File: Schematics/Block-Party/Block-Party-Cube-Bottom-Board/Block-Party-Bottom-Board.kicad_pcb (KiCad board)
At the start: 2 copper layers, 40 x 40 mm, 10 parts

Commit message: Revision 1.01 of the PCBs
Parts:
- removed J1, J2, J3, J4: ~, Connector_PinHeader_2.54mm:PinHeader_1x01_P2.54mm_Vertical
- added J6: YTC-A1001LF-04A, adafruit-jst-4328:ADAFRUIT_4328, F.Cu at (159.2, 77.3)
- added TP1: Diode5V, TestPoint:TestPoint_Pad_D1.0mm, F.Cu at (170.7, 80.6)
- added TP2: DODI, TestPoint:TestPoint_Pad_D1.0mm, F.Cu at (155.2, 81.1)
- added TP4: DO, TestPoint:TestPoint_Pad_D1.0mm, F.Cu at (161.7, 82.1)
- added TP5: 5V, TestPoint:TestPoint_Pad_D1.0mm, F.Cu at (161.7, 86.6)
- added TP6: DI, TestPoint:TestPoint_Pad_D1.0mm, F.Cu at (152.7, 79.1)
- moved LED1 10.4 mm to (159.2, 82.6), turned to -90 degrees
- moved D1 10.0 mm to (168.2, 78.1)
- moved R1 9.49 mm to (164.2, 80.6), turned to 90 degrees
- moved LED2 7.90 mm to (159.4, 73.1), turned to -90 degrees
- moved C1 6.04 mm to (165.2, 76.6), turned to 180 degrees
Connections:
- J5 pad 5: (no net) -> unconnected-(J5-HOLE-Pad5)_1
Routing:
- net D5V: track 64.5 -> 24.6 mm
- net Net-(LED1-DI): track 52.4 -> 15.4 mm
- net DIN: track 48.3 -> 15.2 mm, vias 0 -> 2
- net DOUT: track 33.9 -> 2.77 mm
- net +5V: track 47.4 -> 20.6 mm
- net SENSE: track 43.4 -> 22.4 mm, vias 0 -> 2
- net GND: track 6.66 -> 23.5 mm
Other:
- outline, holes or cut-outs redrawn

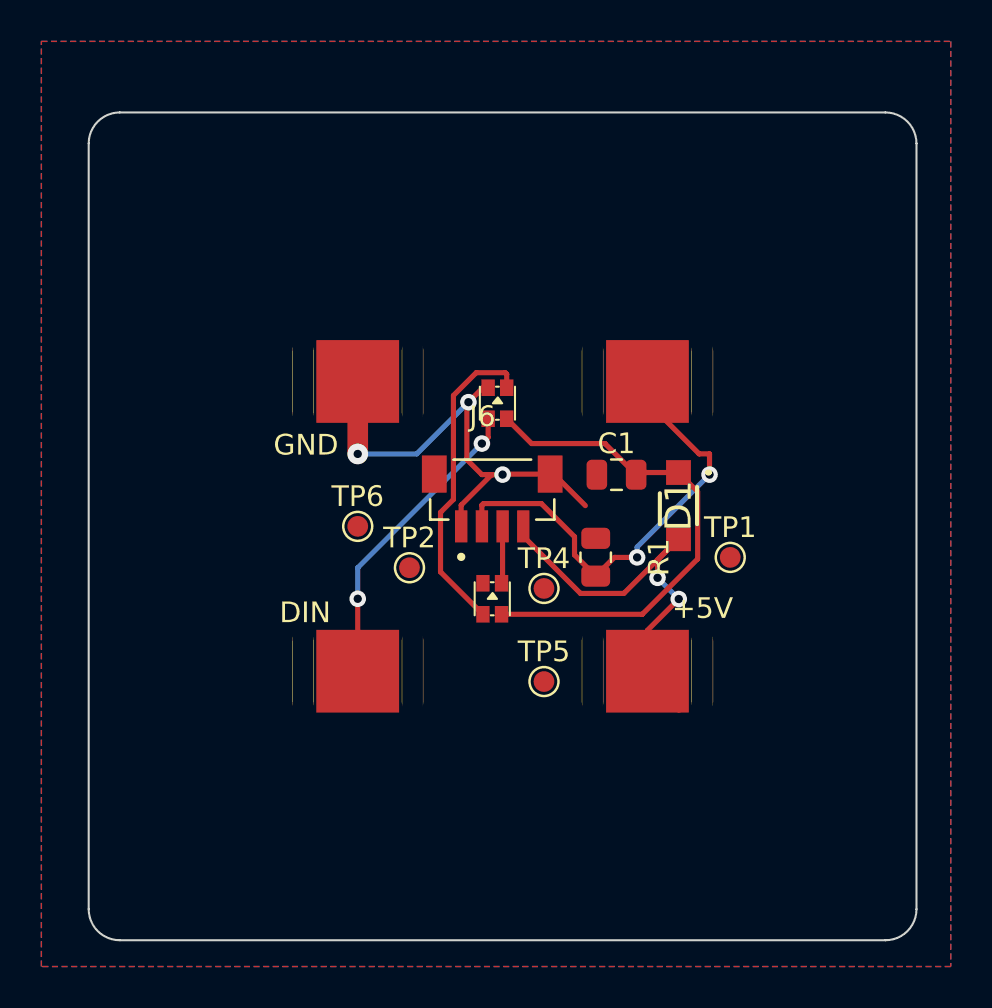
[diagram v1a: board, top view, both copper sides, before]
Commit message: Found a good jst part number and updated the BOMs
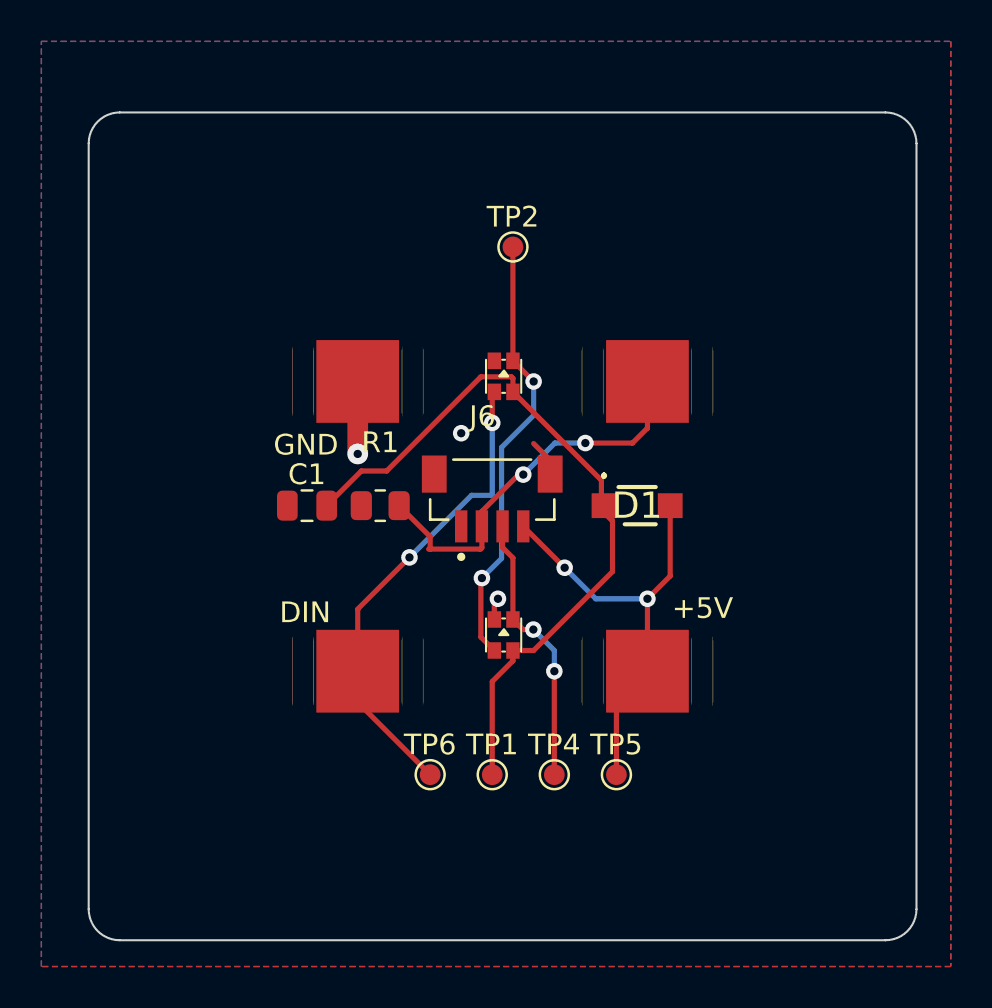
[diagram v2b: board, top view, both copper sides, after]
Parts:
- moved TP2 16.3 mm to (160.2, 65.6)
- moved TP1 15.6 mm to (159.2, 91.1)
- moved C1 15.0 mm to (150.2, 78.1)
- moved TP6 12.5 mm to (156.2, 91.1)
- moved R1 10.7 mm to (153.8, 78.1), turned to 180 degrees
- moved TP4 9.01 mm to (162.2, 91.1)
- moved TP5 5.70 mm to (165.2, 91.1)
- moved D1 2.00 mm to (166.2, 78.1), turned to 0 degrees
- moved LED1 1.83 mm to (159.8, 84.3)
- moved LED2 1.33 mm to (159.8, 71.8)
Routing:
- net GND: track 23.5 -> 5.63 mm
- net D5V: track 24.6 -> 35.8 mm
- net DOUT: track 2.77 -> 13.3 mm, vias 0 -> 2
- net DIN: track 15.2 -> 23.3 mm
- net Net-(LED1-DI): track 15.4 -> 21.2 mm, vias 0 -> 2
- net SENSE: track 22.4 -> 19.0 mm
- net +5V: track 20.6 -> 23.7 mm

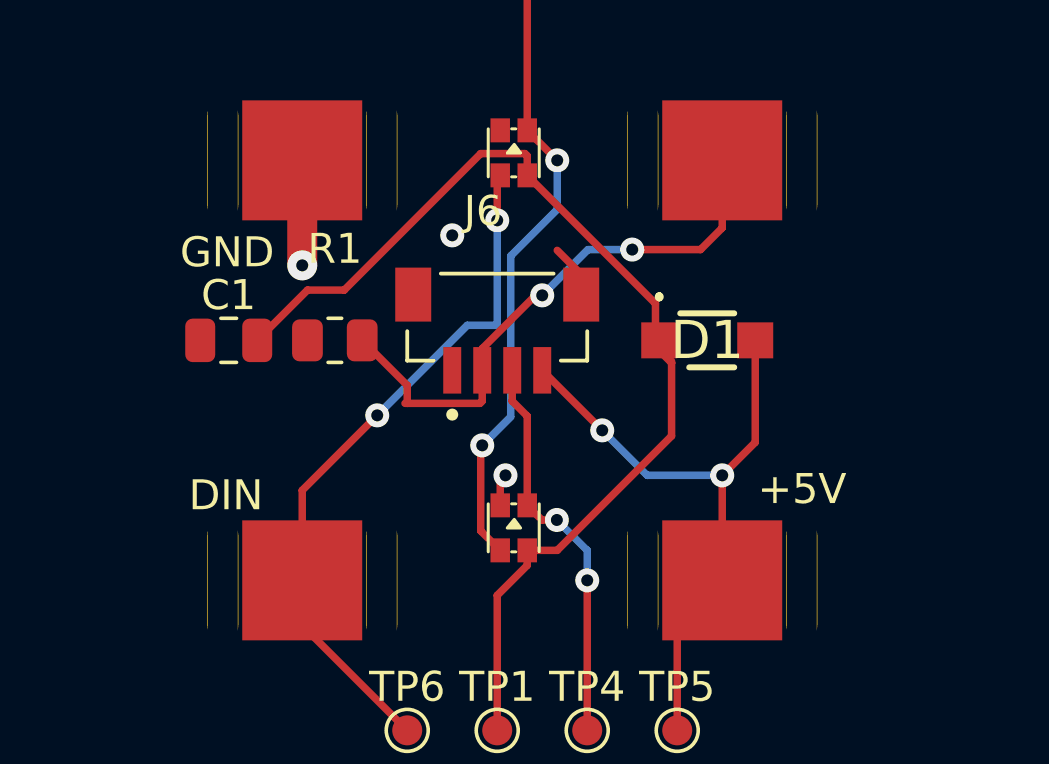
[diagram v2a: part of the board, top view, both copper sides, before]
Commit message: Made the top and bottom PCB the same size
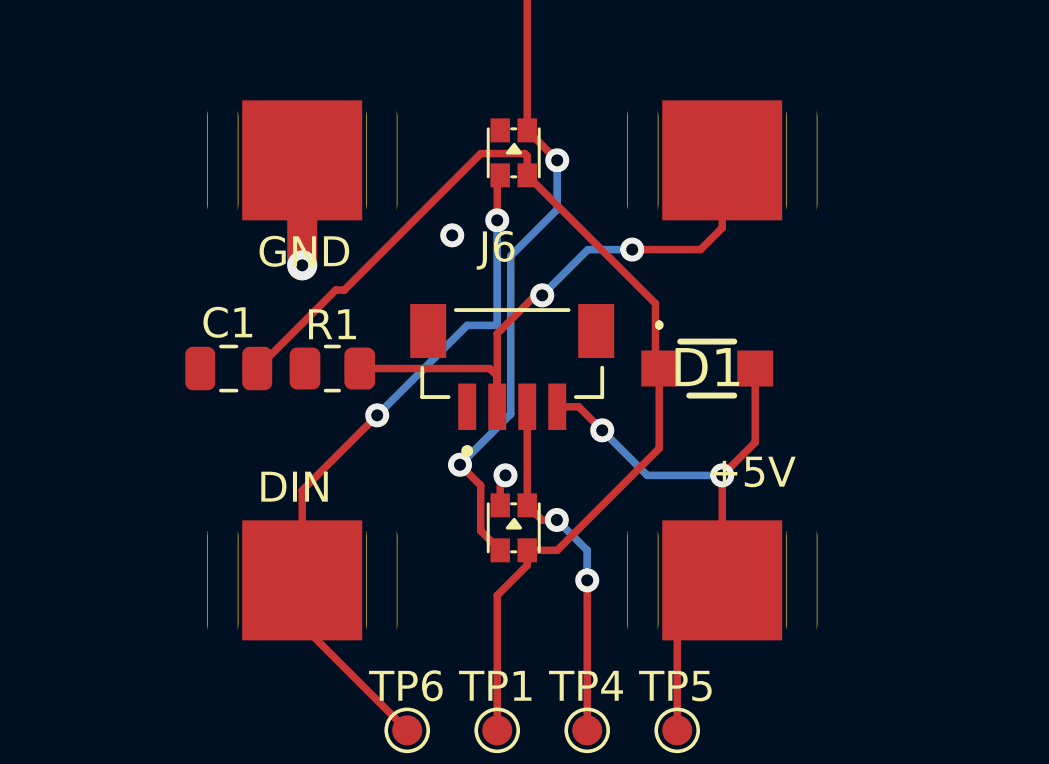
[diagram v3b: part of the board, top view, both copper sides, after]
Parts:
- moved J6 1.31 mm to (159.7, 78.5)
- moved R1 0.94 mm to (153.7, 79.0)
- moved C1 0.94 mm to (150.2, 79.0)
- moved D1 0.94 mm to (166.2, 79.0)
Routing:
- net +5V: track 23.7 -> 19.6 mm
- net GND: track 5.63 -> 3.82 mm
- net DOUT: track 13.3 -> 11.6 mm
- net Net-(LED1-DI): track 21.2 -> 21.8 mm

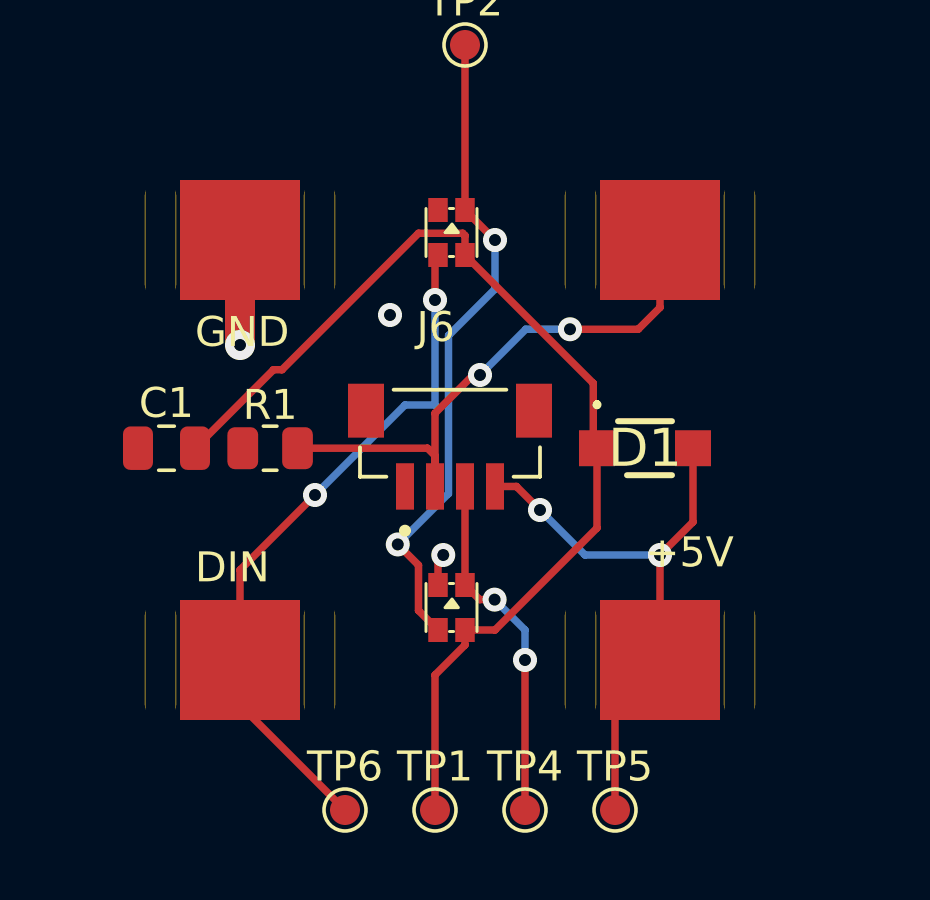
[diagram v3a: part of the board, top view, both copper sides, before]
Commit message: Added bottom pads to the bottom block PCB
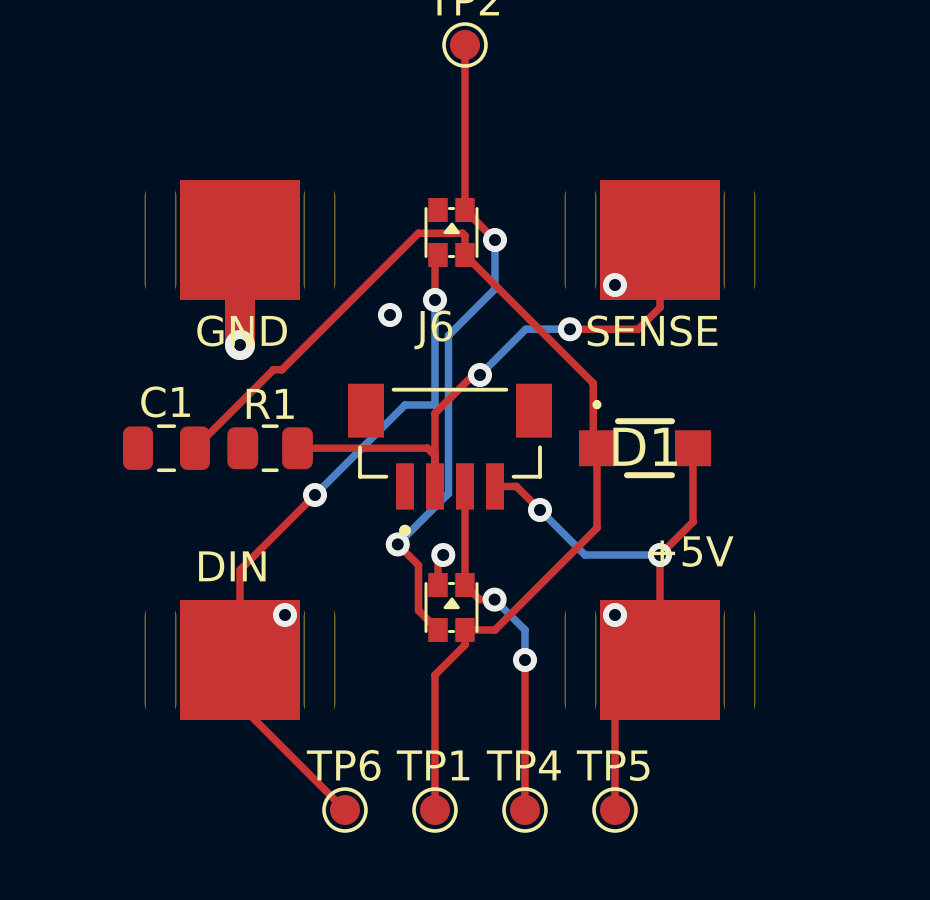
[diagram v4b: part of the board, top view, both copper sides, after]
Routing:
- net GND: track 3.82 -> 6.20 mm
- net SENSE: vias 2 -> 3
- net DIN: vias 2 -> 3
- net +5V: vias 2 -> 3
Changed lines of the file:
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@@
 	(net 7 "Net-(LED1-DI)")
 	(net 8 "unconnected-(J5-HOLE-Pad5)")
-	(net 9 "unconnected-(J5-HOLE-Pad5)_0")
-	(net 10 "unconnected-(J5-HOLE-Pad5)_1")
-	(net 11 "unconnected-(J5-HOLE-Pad5)_2")
-	(net 12 "unconnected-(J5-HOLE-Pad5)_3")
-	(net 13 "unconnected-(J5-HOLE-Pad5)_4")
-	(net 14 "unconnected-(J5-HOLE-Pad5)_5")
-	(net 15 "unconnected-(J5-HOLE-Pad5)_6")
 	(footprint "TestPoint:TestPoint_Pad_D1.0mm"
 		(layer "F.Cu")
@@
 			)
 		)
-		(sheetname "Root")
-		(sheetfile "Block-Party-Bottom-Board.kicad_sch")
 		(attr smd exclude_from_bom dnp)
 		(fp_rect
@@
 			(layer "F.CrtYd")
 		)
+		(fp_text user "GND"
+			(at -8.5 -3.347092 0)
+			(unlocked yes)
+			(layer "F.SilkS")
+			(effects
+				(font
+					(size 1 1)
+					(thickness 0.1)
+				)
+				(justify left bottom)
+			)
+		)
 		(fp_text user "+5V"
 			(at 6.5 4 0)
@@
 			)
 		)
-		(fp_text user "GND"
-			(at -8.5 -3.347092 0)
-			(unlocked yes)
-			(layer "F.SilkS")
-			(effects
-				(font
-					(size 1 1)
-					(thickness 0.1)
-				)
-				(justify left bottom)
-			)
-		)
 		(fp_text user "DIN"
 			(at -8.5 4.5 0)
@@
 				)
 				(justify left bottom)
+			)
+		)
+		(fp_text user "SENSE"
+			(at 4.5 -3.347092 0)
+			(unlocked yes)
+			(layer "F.SilkS")
+			(effects
+				(font
+					(size 1 1)
+					(thickness 0.1)
+				)
+				(justify left bottom)
+			)
+		)
+		(fp_text user "${REFERENCE}"
+			(at 0 -17.78 0)
+			(unlocked yes)
+			(layer "F.Fab")
+			(effects
+				(font
+					(size 1 1)
+					(thickness 0.15)
+				)
 			)
 		)
@@
 			(thermal_bridge_angle 45)
 		)
+		(pad "1" smd rect
+			(at -7 -7)
+			(size 4 4)
+			(layers "B.Cu" "F.Paste" "F.Mask")
+			(net 2 "GND")
+			(pinfunction "GND")
+			(pintype "power_in")
+			(clearance 0.001)
+			(thermal_bridge_angle 45)
+		)
 		(pad "2" smd rect
 			(at 7 -7)
@@
 			(thermal_bridge_angle 45)
 		)
+		(pad "2" smd rect
+			(at 7 -7)
+			(size 4 4)
+			(layers "B.Cu" "F.Paste" "F.Mask")
+			(net 5 "SENSE")
+			(pinfunction "SIG")
+			(pintype "output")
+			(clearance 0.001)
+			(thermal_bridge_angle 45)
+		)
 		(pad "3" smd rect
 			(at -7 7)
@@
 			(thermal_bridge_angle 45)
 		)
+		(pad "3" smd rect
+			(at -7 7)
+			(size 4 4)
+			(layers "B.Cu" "F.Paste" "F.Mask")
+			(net 6 "DIN")
+			(pinfunction "DIN")
+			(pintype "input")
+			(clearance 0.001)
+			(thermal_bridge_angle 45)
+		)
 		(pad "4" smd rect
 			(at 7 7)
 			(size 4 4)
 			(layers "F.Cu" "F.Paste" "F.Mask")
+			(net 3 "+5V")
+			(pinfunction "+5V")
+			(pintype "power_in")
+			(clearance 0.001)
+			(thermal_bridge_angle 45)
+		)
+		(pad "4" smd rect
+			(at 7 7)
+			(size 4 4)
+			(layers "B.Cu" "F.Paste" "F.Mask")
 			(net 3 "+5V")
 			(pinfunction "+5V")
@@
 			(layers "*.Cu" "*.Mask")
 			(remove_unused_layers no)
-			(net 12 "unconnected-(J5-HOLE-Pad5)_3")
+			(net 8 "unconnected-(J5-HOLE-Pad5)")
 			(pinfunction "HOLE")
 			(pintype "output+no_connect")
@@
 			(layers "*.Cu" "*.Mask")
 			(remove_unused_layers no)
-			(net 9 "unconnected-(J5-HOLE-Pad5)_0")
+			(net 8 "unconnected-(J5-HOLE-Pad5)")
 			(pinfunction "HOLE")
 			(pintype "output+no_connect")
@@
 			(layers "*.Cu" "*.Mask")
 			(remove_unused_layers no)
-			(net 11 "unconnected-(J5-HOLE-Pad5)_2")
+			(net 8 "unconnected-(J5-HOLE-Pad5)")
 			(pinfunction "HOLE")
 			(pintype "output+no_connect")
@@
 			(layers "*.Cu" "*.Mask")
 			(remove_unused_layers no)
-			(net 15 "unconnected-(J5-HOLE-Pad5)_6")
+			(net 8 "unconnected-(J5-HOLE-Pad5)")
 			(pinfunction "HOLE")
 			(pintype "output+no_connect")
@@
 			(layers "*.Cu" "*.Mask")
 			(remove_unused_layers no)
-			(net 13 "unconnected-(J5-HOLE-Pad5)_4")
+			(net 8 "unconnected-(J5-HOLE-Pad5)")
 			(pinfunction "HOLE")
 			(pintype "output+no_connect")
@@
 			(layers "*.Cu" "*.Mask")
 			(remove_unused_layers no)
-			(net 14 "unconnected-(J5-HOLE-Pad5)_5")
+			(net 8 "unconnected-(J5-HOLE-Pad5)")
 			(pinfunction "HOLE")
 			(pintype "output+no_connect")
@@
 			(layers "*.Cu" "*.Mask")
 			(remove_unused_layers no)
-			(net 10 "unconnected-(J5-HOLE-Pad5)_1")
+			(net 8 "unconnected-(J5-HOLE-Pad5)")
 			(pinfunction "HOLE")
 			(pintype "output+no_connect")
@@
 	)
 	(segment
+		(start 152.7 75.56)
+		(end 152.7 73.185)
+		(width 1)
+		(layer "B.Cu")
+		(net 2)
+	)
+	(segment
 		(start 167.8 79)
 		(end 167.8 81.46)
@@
 		(width 0.25)
 		(layer "F.Cu")
+		(net 3)
+	)
+	(via
+		(at 165.2 84.56)
+		(size 0.8)
+		(drill 0.4)
+		(layers "F.Cu" "B.Cu")
 		(net 3)
 	)
@@
 	)
 	(via
+		(at 165.2 73.56)
+		(size 0.8)
+		(drill 0.4)
+		(layers "F.Cu" "B.Cu")
+		(net 5)
+	)
+	(via
 		(at 160.7 76.56)
 		(size 0.8)
@@
 		(size 0.8)
 		(drill 0.4)
+		(layers "F.Cu" "B.Cu")
+		(net 6)
+	)
+	(via
+		(at 154.2 84.56)
+		(size 0.8)
+		(drill 0.4)

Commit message: Updated micro configuration files to match the new micro we're using.
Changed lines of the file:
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@@
 			)
 		)
-		(property ki_fp_filters "Pin* Test*")
-		(sheetname "Root")
-		(sheetfile "Block-Party-Bottom-Board.kicad_sch")
 		(attr exclude_from_pos_files)
 		(fp_circle
@@
 			)
 		)
-		(property ki_fp_filters "Pin* Test*")
-		(sheetname "Root")
-		(sheetfile "Block-Party-Bottom-Board.kicad_sch")
 		(attr exclude_from_pos_files)
 		(fp_circle
@@
 			)
 		)
-		(property ki_fp_filters "Pin* Test*")
-		(sheetname "Root")
-		(sheetfile "Block-Party-Bottom-Board.kicad_sch")
 		(attr exclude_from_pos_files)
 		(fp_circle
@@
 			)
 		)
-		(sheetname "Root")
-		(sheetfile "Block-Party-Bottom-Board.kicad_sch")
 		(attr smd)
 		(fp_line
@@
 			)
 		)
-		(sheetname "Root")
-		(sheetfile "Block-Party-Bottom-Board.kicad_sch")
 		(attr smd)
 		(fp_line
@@
 			(layer "F.CrtYd")
 		)
+		(fp_text user "+5V"
+			(at 6.5 4 0)
+			(unlocked yes)
+			(layer "F.SilkS")
+			(effects
+				(font
+					(size 1 1)
+					(thickness 0.1)
+				)
+				(justify left bottom)
+			)
+		)
+		(fp_text user "DIN"
+			(at -8.5 4.5 0)
+			(unlocked yes)
+			(layer "F.SilkS")
+			(effects
+				(font
+					(size 1 1)
+					(thickness 0.1)
+				)
+				(justify left bottom)
+			)
+		)
 		(fp_text user "GND"
 			(at -8.5 -3.347092 0)
-			(unlocked yes)
-			(layer "F.SilkS")
-			(effects
-				(font
-					(size 1 1)
-					(thickness 0.1)
-				)
-				(justify left bottom)
-			)
-		)
-		(fp_text user "+5V"
-			(at 6.5 4 0)
-			(unlocked yes)
-			(layer "F.SilkS")
-			(effects
-				(font
-					(size 1 1)
-					(thickness 0.1)
-				)
-				(justify left bottom)
-			)
-		)
-		(fp_text user "DIN"
-			(at -8.5 4.5 0)
 			(unlocked yes)
 			(layer "F.SilkS")
@@
 			(at -7 -7)
 			(size 4 4)
-			(layers "B.Cu" "F.Paste" "F.Mask")
+			(layers "B.Cu" "B.Paste" "B.Mask")
 			(net 2 "GND")
 			(pinfunction "GND")
@@
 			(at 7 -7)
 			(size 4 4)
-			(layers "B.Cu" "F.Paste" "F.Mask")
+			(layers "B.Cu" "B.Paste" "B.Mask")
 			(net 5 "SENSE")
 			(pinfunction "SIG")
@@
 			(at -7 7)
 			(size 4 4)
-			(layers "B.Cu" "F.Paste" "F.Mask")
+			(layers "B.Cu" "B.Paste" "B.Mask")
 			(net 6 "DIN")
 			(pinfunction "DIN")
@@
 			(at 7 7)
 			(size 4 4)
-			(layers "B.Cu" "F.Paste" "F.Mask")
+			(layers "B.Cu" "B.Paste" "B.Mask")
 			(net 3 "+5V")
 			(pinfunction "+5V")
@@
 			)
 		)
-		(property ki_fp_filters "C_*")
-		(sheetname "Root")
-		(sheetfile "Block-Party-Bottom-Board.kicad_sch")
 		(attr smd)
 		(fp_line
@@
 			)
 		)
-		(sheetname "Root")
-		(sheetfile "Block-Party-Bottom-Board.kicad_sch")
 		(attr smd)
 		(fp_line
@@
 			)
 		)
-		(property ki_fp_filters "R_*")
-		(sheetname "Root")
-		(sheetfile "Block-Party-Bottom-Board.kicad_sch")
 		(attr smd)
 		(fp_line
@@
 			(size 1.025 1.4)
 			(layers "F.Cu" "F.Paste" "F.Mask")
-			(roundrect_rratio 0.243902439)
+			(roundrect_rratio 0.243902)
 			(net 5 "SENSE")
 			(pintype "passive")
@@
 			(size 1.025 1.4)
 			(layers "F.Cu" "F.Paste" "F.Mask")
-			(roundrect_rratio 0.243902439)
+			(roundrect_rratio 0.243902)
 			(net 2 "GND")
 			(pintype "passive")
@@
 			)
 		)
-		(property ki_fp_filters "Pin* Test*")
-		(sheetname "Root")
-		(sheetfile "Block-Party-Bottom-Board.kicad_sch")
 		(attr exclude_from_pos_files)
 		(fp_circle
@@
 			)
 		)
-		(property ki_fp_filters "Pin* Test*")
-		(sheetname "Root")
-		(sheetfile "Block-Party-Bottom-Board.kicad_sch")
 		(attr exclude_from_pos_files)
 		(fp_circle
